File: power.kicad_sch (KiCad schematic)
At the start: 22 parts, among them IC3001 L7805, P3 POWER, SW101 SW_SPDT

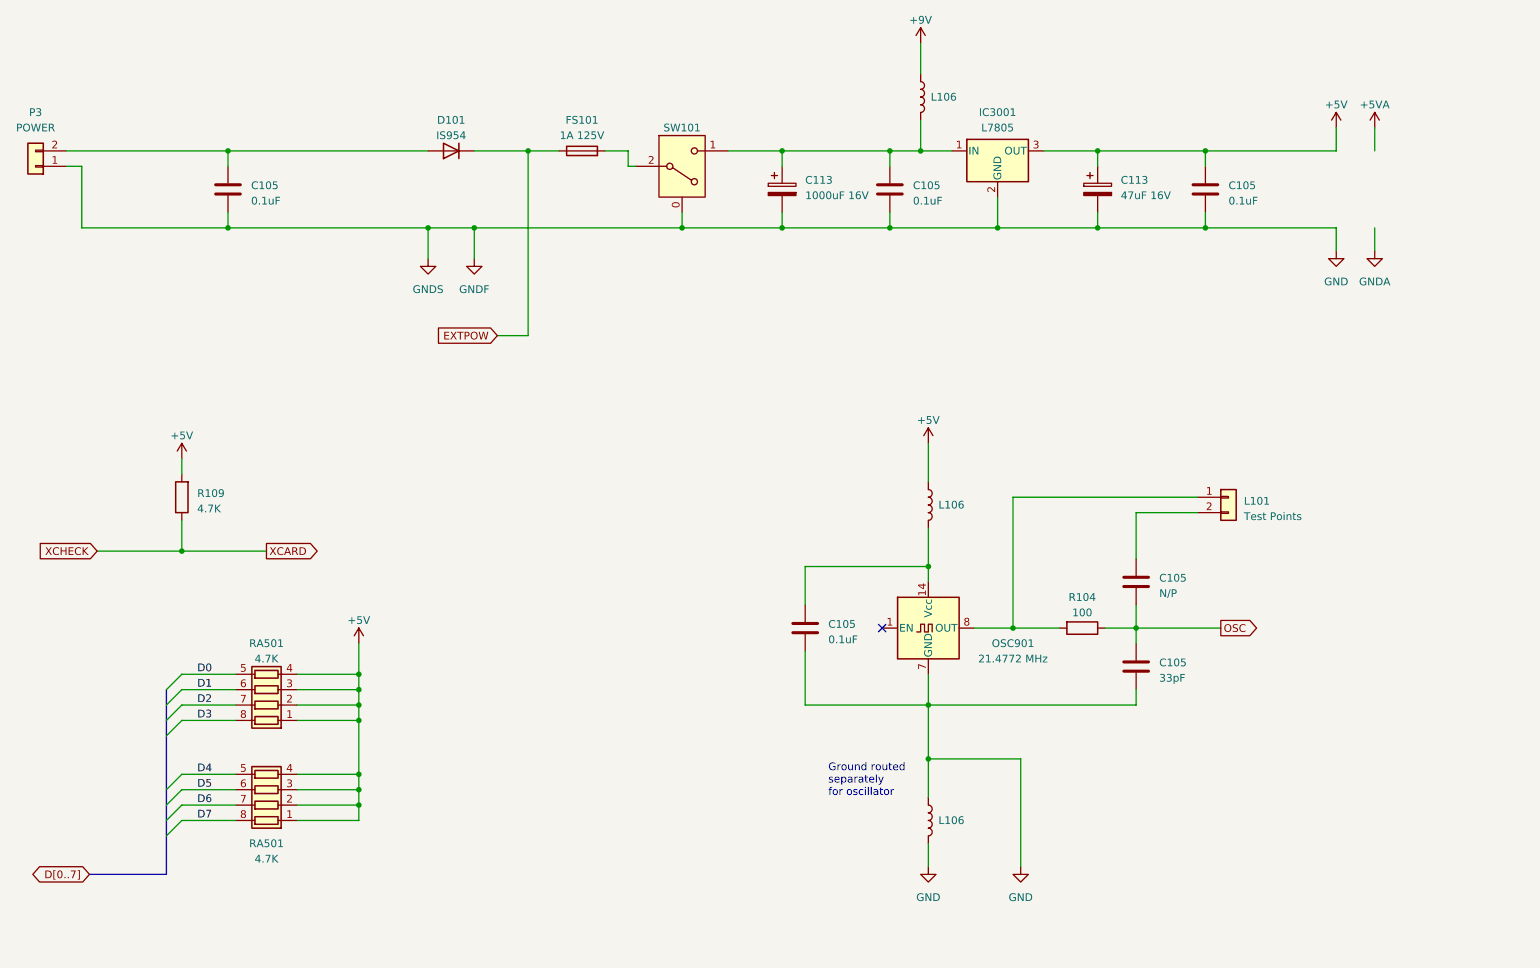
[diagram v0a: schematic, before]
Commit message: Add proper scans, redo traces.
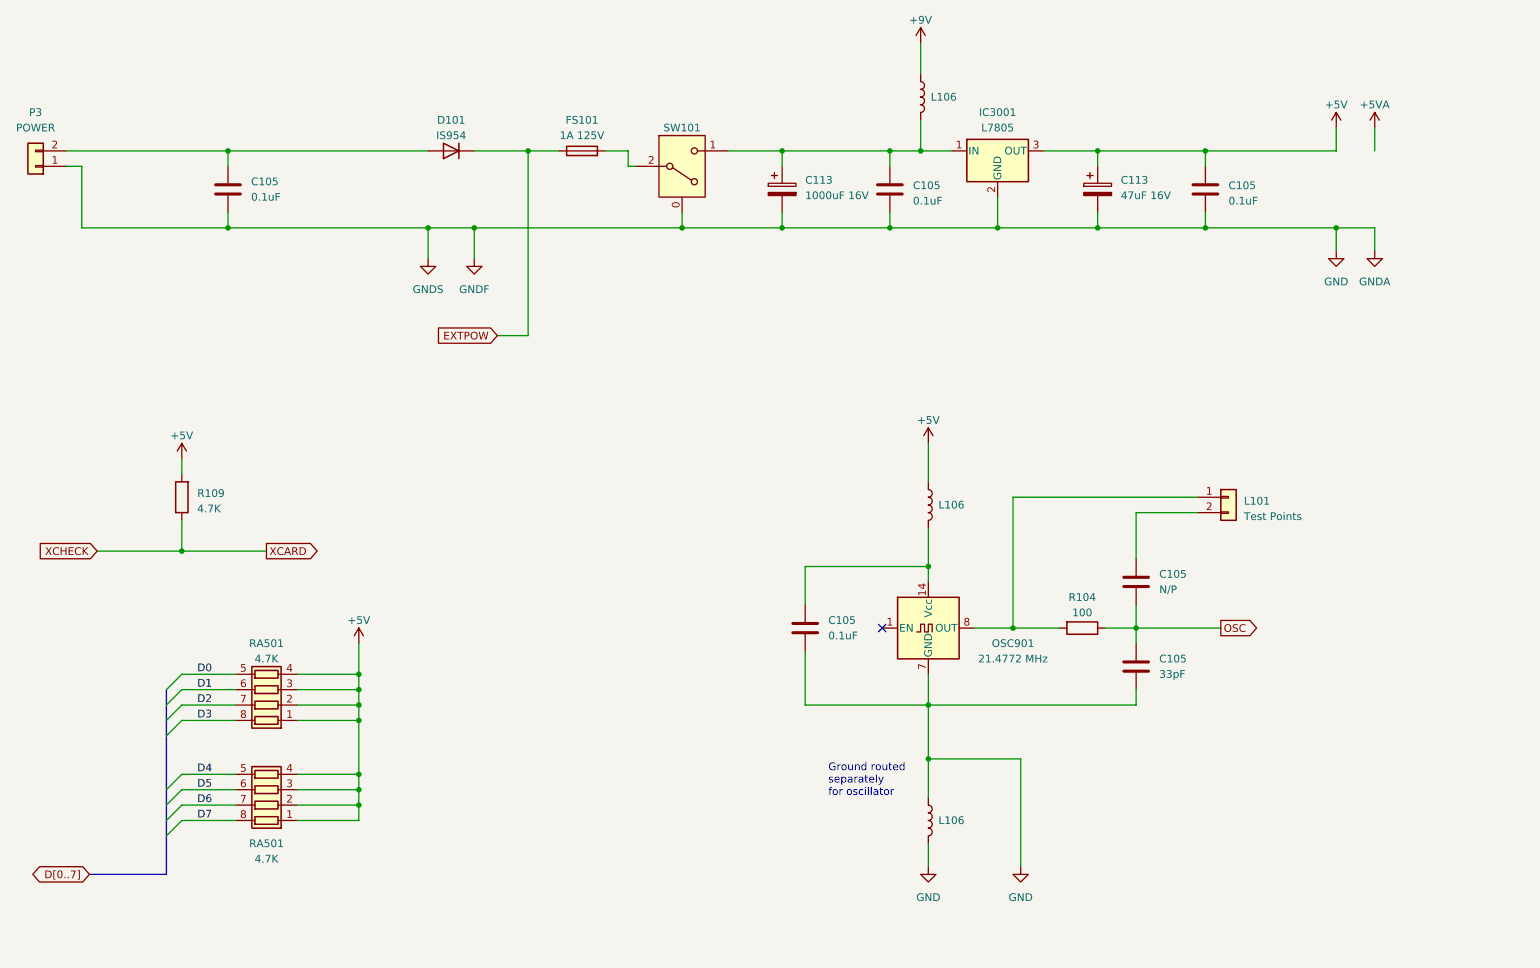
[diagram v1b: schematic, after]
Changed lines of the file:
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@@
   (junction (at 240.03 50.8) (diameter 0) (color 0 0 0 0)
+  )
+  (junction (at 308.61 63.5) (diameter 0) (color 0 0 0 0)
   )
   (junction (at 217.17 50.8) (diameter 0) (color 0 0 0 0)
@@
   )
   (wire (pts (xy 125.73 50.8) (xy 158.75 50.8))
+    (stroke (width 0) (type default))
+  )
+  (wire (pts (xy 308.61 63.5) (xy 314.96 63.5))
     (stroke (width 0) (type default))
   )
@@
   (symbol (lib_id "Device:C") (at 275.59 135.89 0) (unit 1)
     (in_bom yes) (on_board yes) (dnp no) (fields_autoplaced)
-    (property "Reference" "C105" (at 279.4 135.255 0)
-      (effects (font (size 1.27 1.27)) (justify left))
-    )
-    (property "Value" "33pF" (at 279.4 137.795 0)
+    (property "Reference" "C105" (at 279.4 134.62 0)
+      (effects (font (size 1.27 1.27)) (justify left))
+    )
+    (property "Value" "33pF" (at 279.4 137.16 0)
       (effects (font (size 1.27 1.27)) (justify left))
     )
@@
         )
         (path "/c1c718c6-a427-431e-a18b-e46f94ae8e09/ba362b1f-3cb7-4861-9385-2b05dca17551"
-          (reference "C145") (unit 1)
+          (reference "C946") (unit 1)
         )
       )
@@
   (symbol (lib_id "Device:C") (at 275.59 121.92 0) (unit 1)
     (in_bom yes) (on_board yes) (dnp no) (fields_autoplaced)
-    (property "Reference" "C105" (at 279.4 121.285 0)
-      (effects (font (size 1.27 1.27)) (justify left))
-    )
-    (property "Value" "N/P" (at 279.4 123.825 0)
+    (property "Reference" "C105" (at 279.4 120.65 0)
+      (effects (font (size 1.27 1.27)) (justify left))
+    )
+    (property "Value" "N/P" (at 279.4 123.19 0)
       (effects (font (size 1.27 1.27)) (justify left))
     )
@@
         )
         (path "/c1c718c6-a427-431e-a18b-e46f94ae8e09/ba362b1f-3cb7-4861-9385-2b05dca17551"
-          (reference "C153") (unit 1)
+          (reference "C943") (unit 1)
         )
       )
@@
   (symbol (lib_id "Device:C") (at 125.73 57.15 0) (unit 1)
     (in_bom yes) (on_board yes) (dnp no) (fields_autoplaced)
-    (property "Reference" "C105" (at 129.54 56.515 0)
-      (effects (font (size 1.27 1.27)) (justify left))
-    )
-    (property "Value" "0.1uF" (at 129.54 59.055 0)
+    (property "Reference" "C105" (at 129.54 55.88 0)
+      (effects (font (size 1.27 1.27)) (justify left))
+    )
+    (property "Value" "0.1uF" (at 129.54 58.42 0)
       (effects (font (size 1.27 1.27)) (justify left))
     )
@@
         )
         (path "/c1c718c6-a427-431e-a18b-e46f94ae8e09/ba362b1f-3cb7-4861-9385-2b05dca17551"
-          (reference "C148") (unit 1)
+          (reference "C316") (unit 1)
         )
       )
@@
   (symbol (lib_id "Device:C") (at 220.98 129.54 0) (unit 1)
     (in_bom yes) (on_board yes) (dnp no) (fields_autoplaced)
-    (property "Reference" "C105" (at 224.79 128.905 0)
-      (effects (font (size 1.27 1.27)) (justify left))
-    )
-    (property "Value" "0.1uF" (at 224.79 131.445 0)
+    (property "Reference" "C105" (at 224.79 128.27 0)
+      (effects (font (size 1.27 1.27)) (justify left))
+    )
+    (property "Value" "0.1uF" (at 224.79 130.81 0)
       (effects (font (size 1.27 1.27)) (justify left))
     )
@@
         )
         (path "/c1c718c6-a427-431e-a18b-e46f94ae8e09/ba362b1f-3cb7-4861-9385-2b05dca17551"
-          (reference "C146") (unit 1)
-        )
-      )
+          (reference "C942") (unit 1)
+        )
+      )

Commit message: More tracing.
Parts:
- removed R109: 4.7K, Resistor_SMD:R_0805_2012Metric, symbol Device:R
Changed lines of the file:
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@@
   (junction (at 241.3 119.38) (diameter 0) (color 0 0 0 0)
-  )
-  (junction (at 118.11 116.84) (diameter 0) (color 0 0 0 0)
   )
   (junction (at 147.32 137.16) (diameter 0) (color 0 0 0 0)
@@
     (stroke (width 0) (type default))
   )
-  (wire (pts (xy 132.08 116.84) (xy 118.11 116.84))
-    (stroke (width 0) (type default))
-  )
   (wire (pts (xy 101.6 53.34) (xy 101.6 63.5))
     (stroke (width 0) (type default))
   )
-  (wire (pts (xy 118.11 116.84) (xy 118.11 111.76))
-    (stroke (width 0) (type default))
-  )
   (wire (pts (xy 137.16 142.24) (xy 147.32 142.24))
     (stroke (width 0) (type default))
@@
     (stroke (width 0) (type default))
   )
-  (wire (pts (xy 118.11 101.6) (xy 118.11 104.14))
-    (stroke (width 0) (type default))
-  )
   (wire (pts (xy 137.16 137.16) (xy 147.32 137.16))
     (stroke (width 0) (type default))
@@
   )
   (wire (pts (xy 308.61 63.5) (xy 314.96 63.5))
-    (stroke (width 0) (type default))
-  )
-  (wire (pts (xy 104.14 116.84) (xy 118.11 116.84))
     (stroke (width 0) (type default))
   )
@@
   (label "D0" (at 120.65 137.16 0) (fields_autoplaced)
     (effects (font (size 1.27 1.27)) (justify left bottom))
-  )
-  (global_label "XCHECK" (shape input) (at 104.14 116.84 180) (fields_autoplaced)
-    (effects (font (size 1.27 1.27)) (justify right))
-    (property "Intersheetrefs" "${INTERSHEET_REFS}" (at 93.7352 116.84 0)
-      (effects (font (size 1.27 1.27)) (justify right) hide)
-    )
   )
   (global_label "D[0..7]" (shape bidirectional) (at 102.87 170.18 180) (fields_autoplaced)
@@
     (property "Intersheetrefs" "${INTERSHEET_REFS}" (at 92.2609 170.18 0)
       (effects (font (size 1.27 1.27)) (justify right) hide)
-    )
-  )
-  (global_label "XCARD" (shape output) (at 132.08 116.84 0) (fields_autoplaced)
-    (effects (font (size 1.27 1.27)) (justify left))
-    (property "Intersheetrefs" "${INTERSHEET_REFS}" (at 141.0939 116.84 0)
-      (effects (font (size 1.27 1.27)) (justify left) hide)
     )
   )
@@
     )
   )
-  (symbol (lib_id "power:+5V") (at 118.11 101.6 0) (unit 1)
-    (in_bom yes) (on_board yes) (dnp no) (fields_autoplaced)
-    (property "Reference" "#PWR026" (at 118.11 105.41 0)
-      (effects (font (size 1.27 1.27)) hide)
-    )
-    (property "Value" "+5V" (at 118.11 97.79 0)
-      (effects (font (size 1.27 1.27)))
-    )
-    (property "Footprint" "" (at 118.11 101.6 0)
-      (effects (font (size 1.27 1.27)) hide)
-    )
-    (property "Datasheet" "" (at 118.11 101.6 0)
-      (effects (font (size 1.27 1.27)) hide)
-    )
-    (pin "1")
-    (instances
-      (project "PCE"
-        (path "/c1c718c6-a427-431e-a18b-e46f94ae8e09/c78d7e8a-3e65-46f4-91f4-96eb31925bea"
-          (reference "#PWR026") (unit 1)
-        )
-        (path "/c1c718c6-a427-431e-a18b-e46f94ae8e09/ba362b1f-3cb7-4861-9385-2b05dca17551"
-          (reference "#PWR045") (unit 1)
-        )
-      )
-    )
-  )
   (symbol (lib_id "PC-Engine:SW_SPDT") (at 200.66 53.34 0) (unit 1)
     (in_bom yes) (on_board yes) (dnp no)
@@
         )
       )
-    )
-  )
-  (symbol (lib_id "Device:R") (at 118.11 107.95 180) (unit 1)
-    (in_bom yes) (on_board yes) (dnp no) (fields_autoplaced)
-    (property "Reference" "R109" (at 120.65 107.315 0)
-      (effects (font (size 1.27 1.27)) (justify right))
-    )
-    (property "Value" "4.7K" (at 120.65 109.855 0)
-      (effects (font (size 1.27 1.27)) (justify right))
-    )
-    (property "Footprint" "Resistor_SMD:R_0805_2012Metric" (at 119.888 107.95 90)
-      (effects (font (size 1.27 1.27)) hide)
-    )
-    (property "Datasheet" "~" (at 118.11 107.95 0)
-      (effects (font (size 1.27 1.27)) hide)
-    )
-    (pin "1")
-    (pin "2")
-    (instances
-      (project "PCE"
-        (path "/c1c718c6-a427-431e-a18b-e46f94ae8e09/1d91d06a-381a-4a70-bfc1-2abf4d159a91"
-          (reference "R109") (unit 1)
-        )
-        (path "/c1c718c6-a427-431e-a18b-e46f94ae8e09/ba362b1f-3cb7-4861-9385-2b05dca17551"
-          (reference "R101") (unit 1)
-        )
-      )

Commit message: Yet more tracing.
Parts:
- added C113 (x5): ~, A-PCENGINE:Elec_P5.00mm, symbol Device:C_Polarized
- added IC302: L7805, Connector_PinHeader_2.54mm:PinHeader_1x03_P2.54mm_Vertical, symbol Regulator_Linear:L7805
- renumbered IC3001 to IC303, P3 to PX3
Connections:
- net GND: now also C113.2, C113.2, C113.2, C113.2, IC302.2 (GND)
- net at C105.1, C113.1, IC303.1 (IN)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: now also C113.1, IC302.1 (IN)
- new net +5VD: C113.1, IC302.3 (OUT)

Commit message: Power rails, etc.
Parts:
- added Q503: BR 29, Package_TO_SOT_SMD:SOT-23, symbol Device:Q_NPN_BEC
- added R104: ?, Resistor_SMD:R_0805_2012Metric, symbol Device:R
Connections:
- net +5VD: now also Q503.3 (C), R104.1
- net GND: now also C113.2
- new net: Q503.1 (B), R104.2
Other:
- moved on the sheet: C113
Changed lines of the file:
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@@
   (junction (at 147.32 137.16) (diameter 0) (color 0 0 0 0)
+  )
+  (junction (at 310.515 85.09) (diameter 0) (color 0 0 0 0)
   )
   (junction (at 166.37 63.5) (diameter 0) (color 0 0 0 0)
@@
     (stroke (width 0) (type default))
   )
+  (wire (pts (xy 292.735 85.09) (xy 296.545 85.09))
+    (stroke (width 0) (type default))
+  )
   (wire (pts (xy 240.03 50.8) (xy 243.205 50.8))
     (stroke (width 0) (type default))
@@
     (stroke (width 0) (type default))
   )
+  (wire (pts (xy 310.515 85.09) (xy 310.515 72.39))
+    (stroke (width 0) (type default))
+  )
   (bus (pts (xy 115.57 142.24) (xy 115.57 144.78))
     (stroke (width 0) (type default))
@@
     (stroke (width 0) (type default))
   )
+  (wire (pts (xy 231.14 89.535) (xy 238.76 89.535))
+    (stroke (width 0) (type default))
+  )
+  (wire (pts (xy 222.885 85.725) (xy 231.14 85.725))
+    (stroke (width 0) (type default))
+  )
   (wire (pts (xy 275.59 129.54) (xy 275.59 132.08))
     (stroke (width 0) (type default))
@@
     (stroke (width 0) (type default))
   )
+  (wire (pts (xy 231.14 85.725) (xy 231.14 89.535))
+    (stroke (width 0) (type default))
+  )
   (wire (pts (xy 200.66 63.5) (xy 217.17 63.5))
     (stroke (width 0) (type default))
@@
     (stroke (width 0) (type default))
   )
+  (wire (pts (xy 310.515 85.09) (xy 310.515 86.995))
+    (stroke (width 0) (type default))
+  )
   (wire (pts (xy 99.06 50.8) (xy 125.73 50.8))
     (stroke (width 0) (type default))
   )
+  (wire (pts (xy 302.895 92.075) (xy 292.735 92.075))
+    (stroke (width 0) (type default))
+  )
   (wire (pts (xy 240.03 45.72) (xy 240.03 50.8))
     (stroke (width 0) (type default))
@@
     (stroke (width 0) (type default))
   )
+  (wire (pts (xy 238.76 89.535) (xy 238.76 86.995))
+    (stroke (width 0) (type default))
+  )
   (wire (pts (xy 147.32 153.67) (xy 147.32 156.21))
     (stroke (width 0) (type default))
@@
     (stroke (width 0) (type default))
   )
+  (wire (pts (xy 304.165 85.09) (xy 310.515 85.09))
+    (stroke (width 0) (type default))
+  )
   (wire (pts (xy 275.59 139.7) (xy 275.59 142.24))
     (stroke (width 0) (type default))
@@
   )
   (wire (pts (xy 101.6 63.5) (xy 125.73 63.5))
+    (stroke (width 0) (type default))
+  )
+  (wire (pts (xy 310.515 72.39) (xy 289.56 72.39))
+    (stroke (width 0) (type default))
+  )
+  (wire (pts (xy 292.735 92.075) (xy 292.735 85.09))
     (stroke (width 0) (type default))
   )
@@
     )
   )
-  (symbol (lib_id "Device:C_Polarized") (at 117.475 111.125 0) (unit 1)
+  (symbol (lib_id "Device:C_Polarized") (at 238.76 83.185 0) (unit 1)
     (in_bom yes) (on_board yes) (dnp no)
-    (property "Reference" "C113" (at 121.285 109.601 0)
-      (effects (font (size 1.27 1.27)) (justify left))
-    )
-    (property "Value" "~" (at 121.285 112.141 0)
-      (effects (font (size 1.27 1.27)) (justify left))
-    )
-    (property "Footprint" "A-PCENGINE:Elec_P5.00mm" (at 118.4402 114.935 0)
-      (effects (font (size 1.27 1.27)) hide)
-    )
-    (property "Datasheet" "~" (at 117.475 111.125 0)
+    (property "Reference" "C113" (at 242.57 81.661 0)
+      (effects (font (size 1.27 1.27)) (justify left))
+    )
+    (property "Value" "~" (at 242.57 84.201 0)
+      (effects (font (size 1.27 1.27)) (justify left))
+    )
+    (property "Footprint" "A-PCENGINE:Elec_P5.00mm" (at 239.7252 86.995 0)
+      (effects (font (size 1.27 1.27)) hide)
+    )
+    (property "Datasheet" "~" (at 238.76 83.185 0)
       (effects (font (size 1.27 1.27)) hide)
     )
@@
         (path "/c1c718c6-a427-431e-a18b-e46f94ae8e09/ba362b1f-3cb7-4861-9385-2b05dca17551"
           (reference "L101") (unit 1)
+        )
+      )
+    )
+  )
+  (symbol (lib_id "Device:R") (at 300.355 85.09 270) (unit 1)
+    (in_bom yes) (on_board yes) (dnp no)
+    (property "Reference" "R104" (at 300.355 80.01 90)
+      (effects (font (size 1.27 1.27)))
+    )
+    (property "Value" "?" (at 300.355 82.55 90)
+      (effects (font (size 1.27 1.27)))
+    )
+    (property "Footprint" "Resistor_SMD:R_0805_2012Metric" (at 300.355 83.312 90)
+      (effects (font (size 1.27 1.27)) hide)
+    )
+    (property "Datasheet" "~" (at 300.355 85.09 0)
+      (effects (font (size 1.27 1.27)) hide)
+    )
+    (pin "1")
+    (pin "2")
+    (instances
+      (project "PCE"
+        (path "/c1c718c6-a427-431e-a18b-e46f94ae8e09/1d91d06a-381a-4a70-bfc1-2abf4d159a91"
+          (reference "R104") (unit 1)
+        )
+        (path "/c1c718c6-a427-431e-a18b-e46f94ae8e09/c78d7e8a-3e65-46f4-91f4-96eb31925bea"
+          (reference "R113") (unit 1)
+        )
+        (path "/c1c718c6-a427-431e-a18b-e46f94ae8e09/ba362b1f-3cb7-4861-9385-2b05dca17551"
+          (reference "R309") (unit 1)
         )
       )
@@
         )
       )
+    )
+  )
+  (symbol (lib_id "Device:Q_NPN_BEC") (at 307.975 92.075 0) (unit 1)
+    (in_bom yes) (on_board yes) (dnp no) (fields_autoplaced)
+    (property "Reference" "Q503" (at 313.69 90.805 0)
+      (effects (font (size 1.27 1.27)) (justify left))
+    )
+    (property "Value" "BR 29" (at 313.69 93.345 0)
+      (effects (font (size 1.27 1.27)) (justify left))
+    )
+    (property "Footprint" "Package_TO_SOT_SMD:SOT-23" (at 313.055 89.535 0)
+      (effects (font (size 1.27 1.27)) hide)
+    )
+    (property "Datasheet" "~" (at 307.975 92.075 0)
+      (effects (font (size 1.27 1.27)) hide)
+    )
+    (pin "1")
+    (pin "2")
+    (pin "3")
+    (instances
+      (project "PCE"
+        (path "/c1c718c6-a427-431e-a18b-e46f94ae8e09/ba362b1f-3cb7-4861-9385-2b05dca17551"
+          (reference "Q503") (unit 1)
+        )
+      )
